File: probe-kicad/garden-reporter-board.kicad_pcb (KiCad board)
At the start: 2 copper layers, 40.6 x 88.9 mm, 21 parts, among them J1 70543-0106, J2 Conn_01x02, J3 70543-0002, J4 70543-0002, J5 70543-0002, Q1 TN0702N3-G, U1 MCP1700-3302E_TO92, U2 MCP1700-3302E_TO92

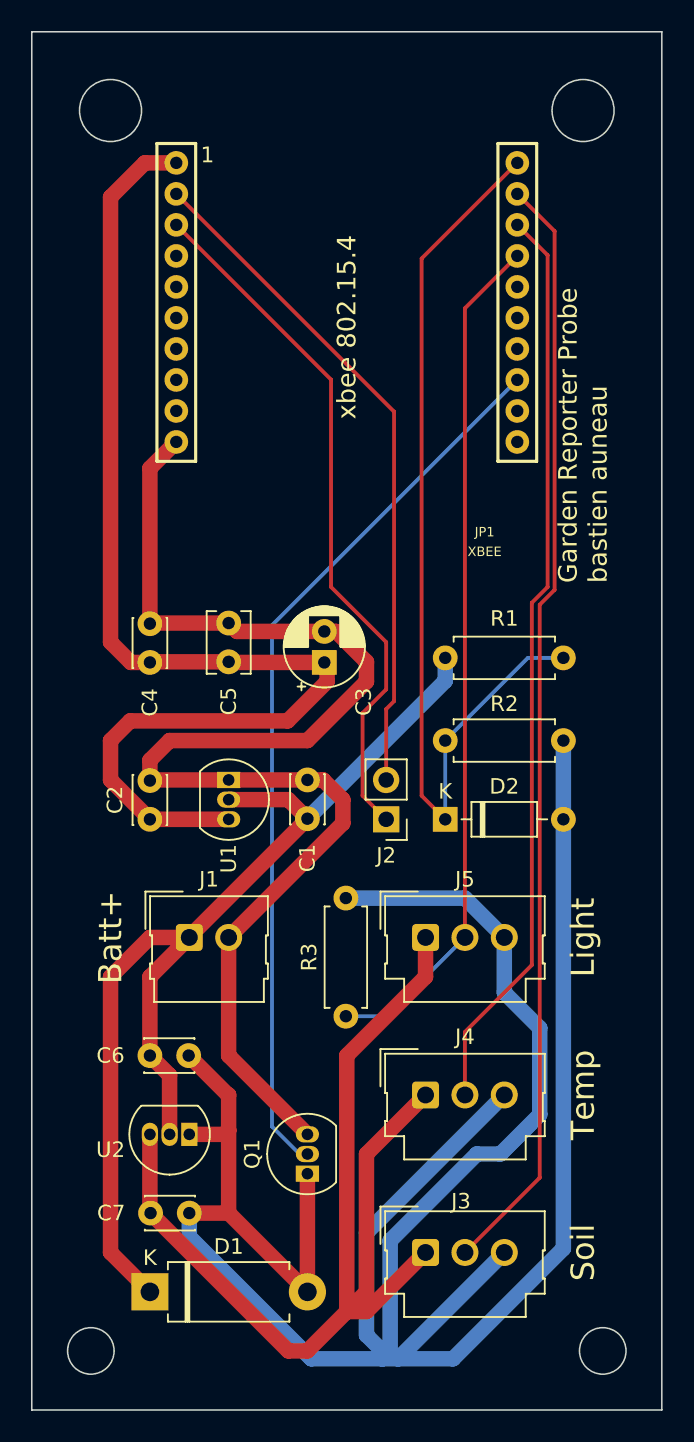
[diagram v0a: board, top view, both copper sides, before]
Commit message: Fix bad flyback diode connection, move xbee edge drawing to fron silkscreen
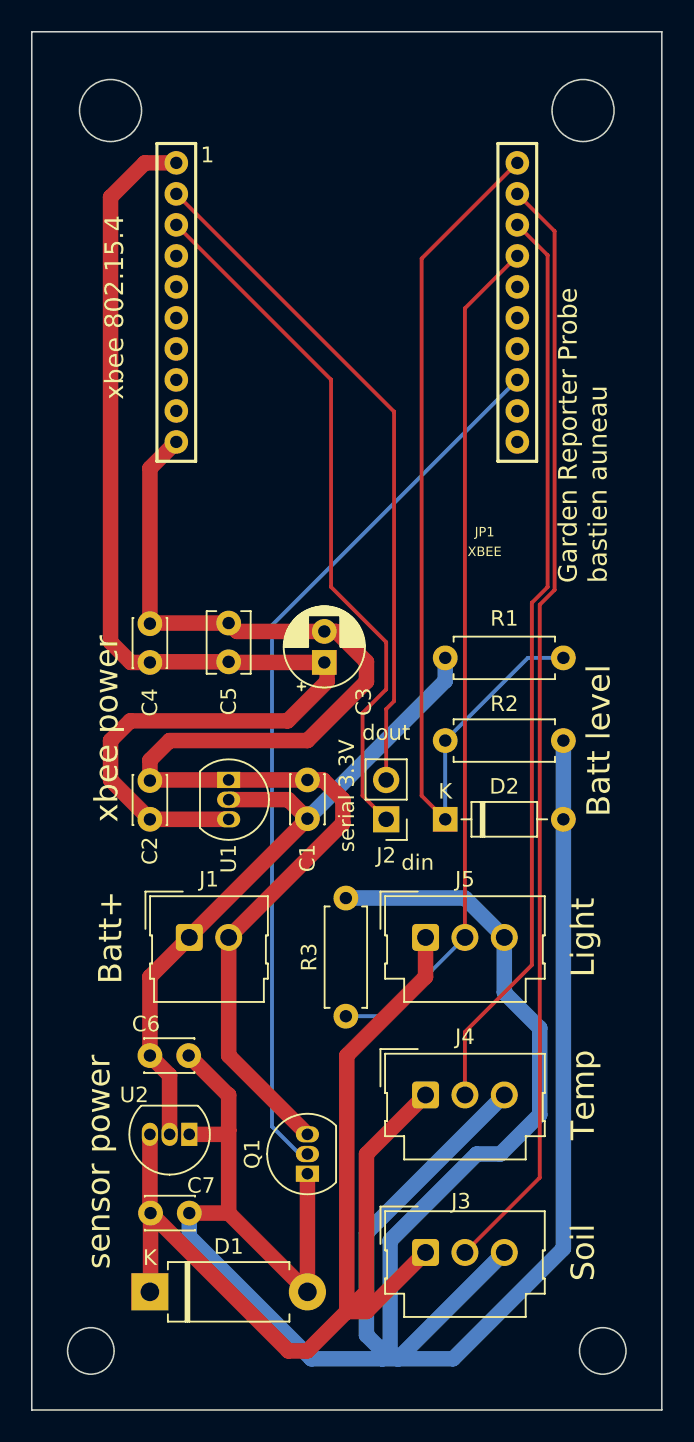
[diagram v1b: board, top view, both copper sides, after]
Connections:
- D1 pad 1: +BATT -> +3.3VADC
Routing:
- net +BATT: track 72.2 -> 44.7 mm
- net +3.3VADC: track 71.5 -> 76.6 mm
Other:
- board text added: "Batt level"
- board text added: "din"
- board text added: "dout"
- board text added: "sensor power"
- board text added: "serial 3.3V"
- board text added: "xbee power"
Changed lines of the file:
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@@
     )
     (fp_line (start -9.74852 -21.24964) (end -12.24788 -21.24964) (layer "F.SilkS") (width 0.2032))
-    (fp_line (start 9.74852 -21.24964) (end 12.24788 -21.24964) (layer "F.SilkS") (width 0.2032))
-    (fp_line (start -12.24788 -0.7493) (end -9.74852 -0.7493) (layer "F.SilkS") (width 0.2032))
-    (fp_line (start 12.24788 -0.7493) (end 9.74852 -0.7493) (layer "F.SilkS") (width 0.2032))
-    (fp_line (start -9.74852 -21.24964) (end -9.74852 -0.7493) (layer "F.SilkS") (width 0.2032))
     (fp_line (start 9.74852 -21.24964) (end 9.74852 -0.7493) (layer "F.SilkS") (width 0.2032))
     (fp_line (start -12.24788 -21.24964) (end -12.24788 -0.7493) (layer "F.SilkS") (width 0.2032))
+    (fp_line (start 12.24788 -0.7493) (end 9.74852 -0.7493) (layer "F.SilkS") (width 0.2032))
+    (fp_line (start -12.24788 -0.7493) (end -9.74852 -0.7493) (layer "F.SilkS") (width 0.2032))
+    (fp_line (start -9.74852 -21.24964) (end -9.74852 -0.7493) (layer "F.SilkS") (width 0.2032))
+    (fp_line (start 9.74852 -21.24964) (end 12.24788 -21.24964) (layer "F.SilkS") (width 0.2032))
     (fp_line (start 12.24788 -21.24964) (end 12.24788 -0.7493) (layer "F.SilkS") (width 0.2032))
+    (fp_line (start 12.24788 -21.24964) (end 4.99872 -27.59964) (layer "Dwgs.User") (width 0.127))
+    (fp_line (start -12.24788 -21.24964) (end -4.99872 -27.59964) (layer "Dwgs.User") (width 0.127))
+    (fp_line (start -4.99872 -27.59964) (end 4.99872 -27.59964) (layer "Dwgs.User") (width 0.127))
+    (fp_line (start -12.24788 0) (end 12.24788 0) (layer "Dwgs.User") (width 0.127))
+    (fp_line (start -12.24788 0) (end -12.24788 6.2484) (layer "Dwgs.User") (width 0.127))
+    (fp_line (start -12.24788 -0.7493) (end -12.24788 0) (layer "Dwgs.User") (width 0.127))
     (fp_line (start 12.24788 0) (end 12.24788 6.2484) (layer "Dwgs.User") (width 0.127))
     (fp_line (start 12.24788 -0.7493) (end 12.24788 0) (layer "Dwgs.User") (width 0.127))
     (fp_line (start -12.24788 6.2484) (end 12.24788 6.2484) (layer "Dwgs.User") (width 0.127))
-    (fp_line (start -12.24788 -21.24964) (end -4.99872 -27.59964) (layer "Dwgs.User") (width 0.127))
-    (fp_line (start -12.24788 -0.7493) (end -12.24788 0) (layer "Dwgs.User") (width 0.127))
-    (fp_line (start -4.99872 -27.59964) (end 4.99872 -27.59964) (layer "Dwgs.User") (width 0.127))
-    (fp_line (start -12.24788 0) (end -12.24788 6.2484) (layer "Dwgs.User") (width 0.127))
-    (fp_line (start -12.24788 0) (end 12.24788 0) (layer "Dwgs.User") (width 0.127))
-    (fp_line (start 12.24788 -21.24964) (end 4.99872 -27.59964) (layer "Dwgs.User") (width 0.127))
     (pad "1" thru_hole circle locked (at -10.9982 -19.99996) (size 1.524 1.524) (drill 0.79756) (layers *.Cu *.Mask)
       (net 3 "+3.3V") (pinfunction "VDD") (pintype "power_in") (solder_mask_margin 0.1016))
@@
     (fp_line (start 2.52 -1.8) (end 2.52 1.8) (layer "F.Fab") (width 0.1))
     (pad "1" thru_hole rect (at 0 0) (size 2.4 2.4) (drill 1.2) (layers *.Cu *.Mask)
-      (net 1 "+BATT") (pinfunction "K") (pintype "passive"))
+      (net 5 "+3.3VADC") (pinfunction "K") (pintype "passive"))
     (pad "2" thru_hole oval (at 10.16 0) (size 2.4 2.4) (drill 1.2) (layers *.Cu *.Mask)
       (net 4 "GND1") (pinfunction "A") (pintype "passive"))
@@
     (property "Sheetname" "")
     (attr through_hole)
-    (fp_text reference "U2" (at 5.08 -0.994977) (layer "F.SilkS")
+    (fp_text reference "U2" (at 3.556 2.54) (layer "F.SilkS")
       (effects (font (size 1 1) (thickness 0.15)))
     )
@@
     (property "Sheetname" "")
     (attr through_hole)
-    (fp_text reference "C7" (at -2.54 0) (layer "F.SilkS")
+    (fp_text reference "C7" (at 3.262 -1.778) (layer "F.SilkS")
       (effects (font (size 1 1) (thickness 0.15)))
     )
@@
     (property "Sheetname" "")
     (attr through_hole)
-    (fp_text reference "C6" (at -2.54 0) (layer "F.SilkS")
+    (fp_text reference "C6" (at -0.254 -2.032) (layer "F.SilkS")
       (effects (font (size 1 1) (thickness 0.15)))
     )
@@
     (property "Sheetname" "")
     (attr through_hole)
-    (fp_text reference "C2" (at 1.25 -2.25 90) (layer "F.SilkS")
+    (fp_text reference "C2" (at -2.032 0 90) (layer "F.SilkS")
       (effects (font (size 1 1) (thickness 0.15)))
     )
@@
   (gr_circle (center 168.91 59.69) (end 170.91 59.69) (layer "Edge.Cuts") (width 0.1) (fill none))
   (gr_circle (center 170.18 139.7) (end 171.68 139.7) (layer "Edge.Cuts") (width 0.1) (fill none))
+  (gr_text "xbee power" (at 138.176 99.568 90) (layer "F.SilkS")
+    (effects (font (size 1.5 1.5) (thickness 0.3)))
+  )
+  (gr_text "dout" (at 156.21 99.822) (layer "F.SilkS")
+    (effects (font (size 1 1) (thickness 0.15)))
+  )
+  (gr_text "sensor power" (at 137.668 127.508 90) (layer "F.SilkS")
+    (effects (font (size 1.5 1.5) (thickness 0.3)))
+  )
   (gr_text "Temp" (at 168.91 123.19 90) (layer "F.SilkS")
     (effects (font (size 1.5 1.5) (thickness 0.3)))
@@
     (effects (font (size 1.5 1.5) (thickness 0.3)))
   )
-  (gr_text "xbee 802.15.4" (at 153.67 73.66 90) (layer "F.SilkS")
+  (gr_text "xbee 802.15.4" (at 138.684 72.39 90) (layer "F.SilkS")
     (effects (font (size 1.2 1.2) (thickness 0.15)))
   )
@@
     (effects (font (size 1.5 1.5) (thickness 0.3)))
   )
+  (gr_text "din" (at 158.242 108.204) (layer "F.SilkS")
+    (effects (font (size 1 1) (thickness 0.15)))
+  )
   (gr_text "Garden Reporter Probe\nbastien auneau" (at 168.91 90.17 90) (layer "F.SilkS")
     (effects (font (size 1.2 1.2) (thickness 0.15)) (justify left))
   )
+  (gr_text "Batt level" (at 169.926 100.33 90) (layer "F.SilkS")
+    (effects (font (size 1.5 1.5) (thickness 0.3)))
+  )
+  (gr_text "serial 3.3V" (at 153.67 103.886 90) (layer "F.SilkS")
+    (effects (font (size 1 1) (thickness 0.25)))
+  )
   (segment (start 143.51 112.99) (end 151.13 105.37) (width 1) (layer "F.Cu") (net 1))
   (segment (start 142.24 121.92) (end 142.24 125.73) (width 1) (layer "F.Cu") (net 1))
-  (segment (start 138.43 115.57) (end 140.97 113.03) (width 1) (layer "F.Cu") (net 1))
   (segment (start 143.51 113.03) (end 140.97 115.57) (width 1) (layer "F.Cu") (net 1))
-  (segment (start 140.97 113.03) (end 143.51 113.03) (width 1) (layer "F.Cu") (net 1))
   (segment (start 151.13 105.37) (end 149.9 104.14) (width 1) (layer "F.Cu") (net 1))
-  (segment (start 138.43 133.35) (end 138.43 115.57) (width 1) (layer "F.Cu") (net 1))
   (segment (start 140.97 120.65) (end 142.24 121.92) (width 1) (layer "F.Cu") (net 1))
   (segment (start 143.51 113.03) (end 143.51 112.99) (width 1) (layer "F.Cu") (net 1))
   (segment (start 140.97 115.57) (end 140.97 120.65) (width 1) (layer "F.Cu") (net 1))
   (segment (start 149.9 104.14) (end 146.05 104.14) (width 1) (layer "F.Cu") (net 1))
-  (segment (start 140.97 135.89) (end 138.43 133.35) (width 1) (layer "F.Cu") (net 1))
   (segment (start 160.02 96.48) (end 160.02 94.996) (width 1) (layer "B.Cu") (net 1))
   (segment (start 151.13 105.37) (end 160.02 96.48) (width 1) (layer "B.Cu") (net 1))
@@
   (segment (start 153.67 120.65) (end 158.75 115.57) (width 1) (layer "F.Cu") (net 5))
   (segment (start 153.67 137.16) (end 153.67 120.65) (width 1) (layer "F.Cu") (net 5))
+  (segment (start 141.01 130.81) (end 141.01 135.85) (width 1) (layer "F.Cu") (net 5))
   (segment (start 154.94 135.89) (end 154.94 127) (width 1) (layer "F.Cu") (net 5))
   (segment (start 154.94 127) (end 158.75 123.19) (width 1) (layer "F.Cu") (net 5))
@@
   (segment (start 153.67 137.16) (end 154.94 135.89) (width 1) (layer "F.Cu") (net 5))
   (segment (start 141.01 130.81) (end 149.9 139.7) (width 1) (layer "F.Cu") (net 5))
+  (segment (start 141.01 135.85) (end 140.97 135.89) (width 1) (layer "F.Cu") (net 5))
   (segment (start 140.97 125.73) (end 140.97 130.77) (width 1) (layer "F.Cu") (net 5))
   (segment (start 158.75 115.57) (end 158.75 113.03) (width 1) (layer "F.Cu") (net 5))

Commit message: Add artichoke picture, add and ùake pretty silkscreen comments
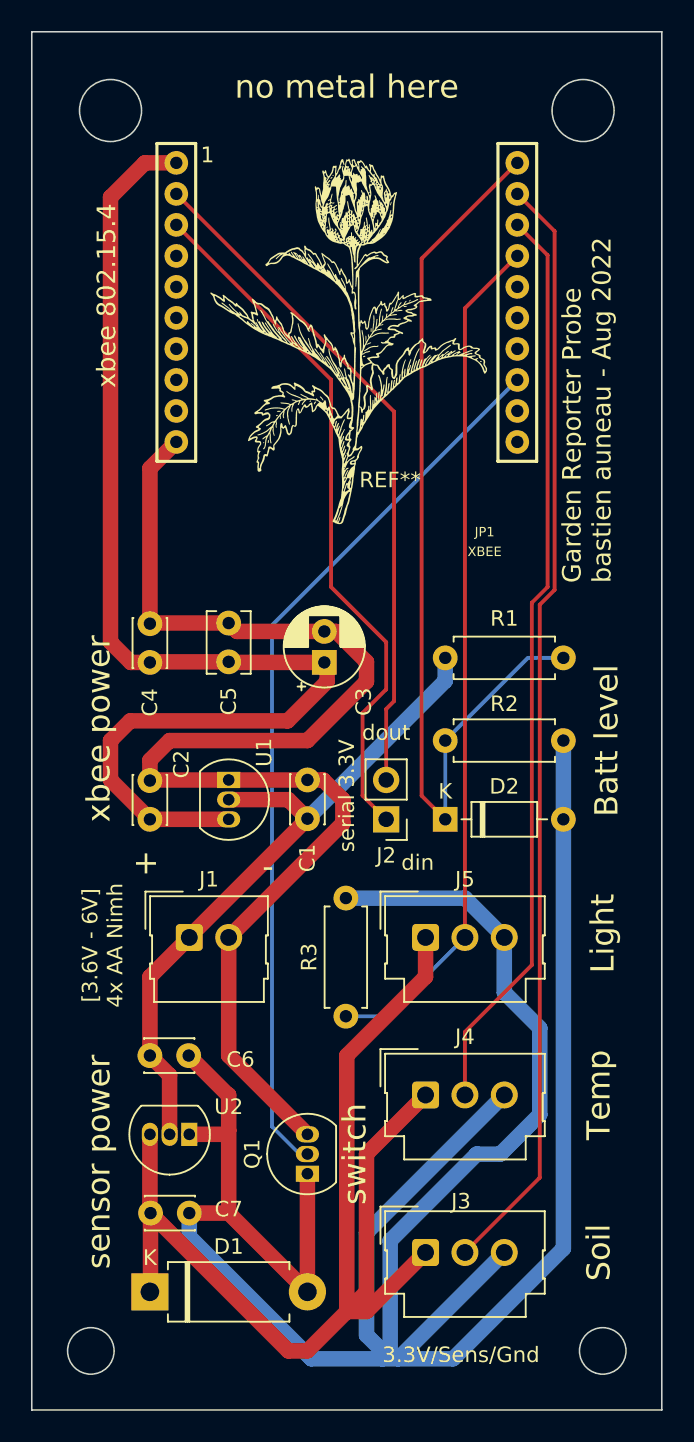
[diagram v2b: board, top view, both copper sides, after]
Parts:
- added REF**: Artichaut, Library_bastien:Artichaut, F.Cu at (153.9, 86.6)
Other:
- board text added: "+"
- board text added: "-"
- board text added: "3.3V/Sens/Gnd"
- board text added: "Garden Reporter Probe bastien auneau - Aug 2022"
- board text added: "[3.6V - 6V] 4x AA Nimh"
- board text added: "no metal here"
- board text added: "switch"
- board text removed: "Batt+"
- board text removed: "Garden Reporter Probe bastien auneau"

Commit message: Pretty
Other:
- board text added: "no metal here !"
- board text removed: "no metal here"
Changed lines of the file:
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@@
     (effects (font (size 1.5 1.5) (thickness 0.3)))
   )
-  (gr_text "no metal here" (at 153.67 58.166) (layer "F.SilkS")
+  (gr_text "no metal here !" (at 153.67 58.166) (layer "F.SilkS")
     (effects (font (size 1.5 1.5) (thickness 0.3)))
   )

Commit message: Feature/better doc
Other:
- board text added: "**rotate** |---->"
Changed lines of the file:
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@@
     (effects (font (size 1.5 1.5) (thickness 0.3)))
+  )
+  (gr_text "**rotate**\n|---->" (at 150.114 121.1072 270) (layer "F.SilkS")
+    (effects (font (size 1 1) (thickness 0.15)))
   )
   (gr_text "Light" (at 170.18 112.776 90) (layer "F.SilkS")
